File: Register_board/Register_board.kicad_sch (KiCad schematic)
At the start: 26 parts, among them J1 Conn_02x32_Odd_Even, U1 74LS374, U10 74LS181, U11 74LS181, U12 74LS374, U13 74LS374, U14 74LS374, U15 74LS374, U16 74LS244, U2 74LS374, U3 74LS374, U4 74LS374, U5 74LS244, U6 74LS374, U7 74LS374, U8 74LS244, U9 74LS75

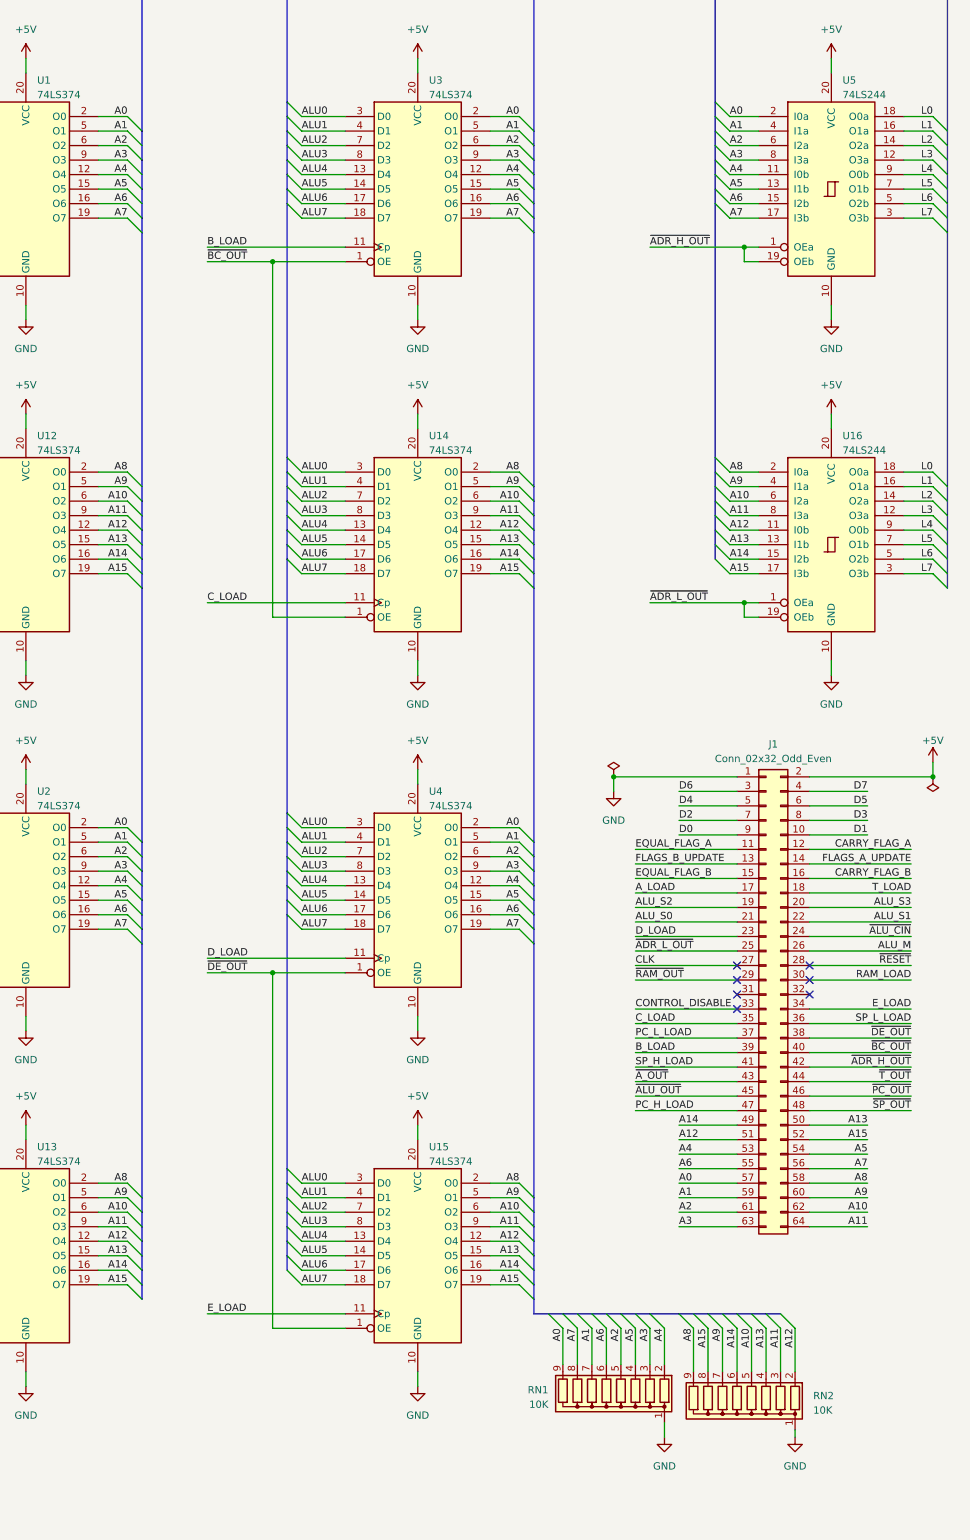
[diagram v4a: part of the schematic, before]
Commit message: Fix address line labelling error
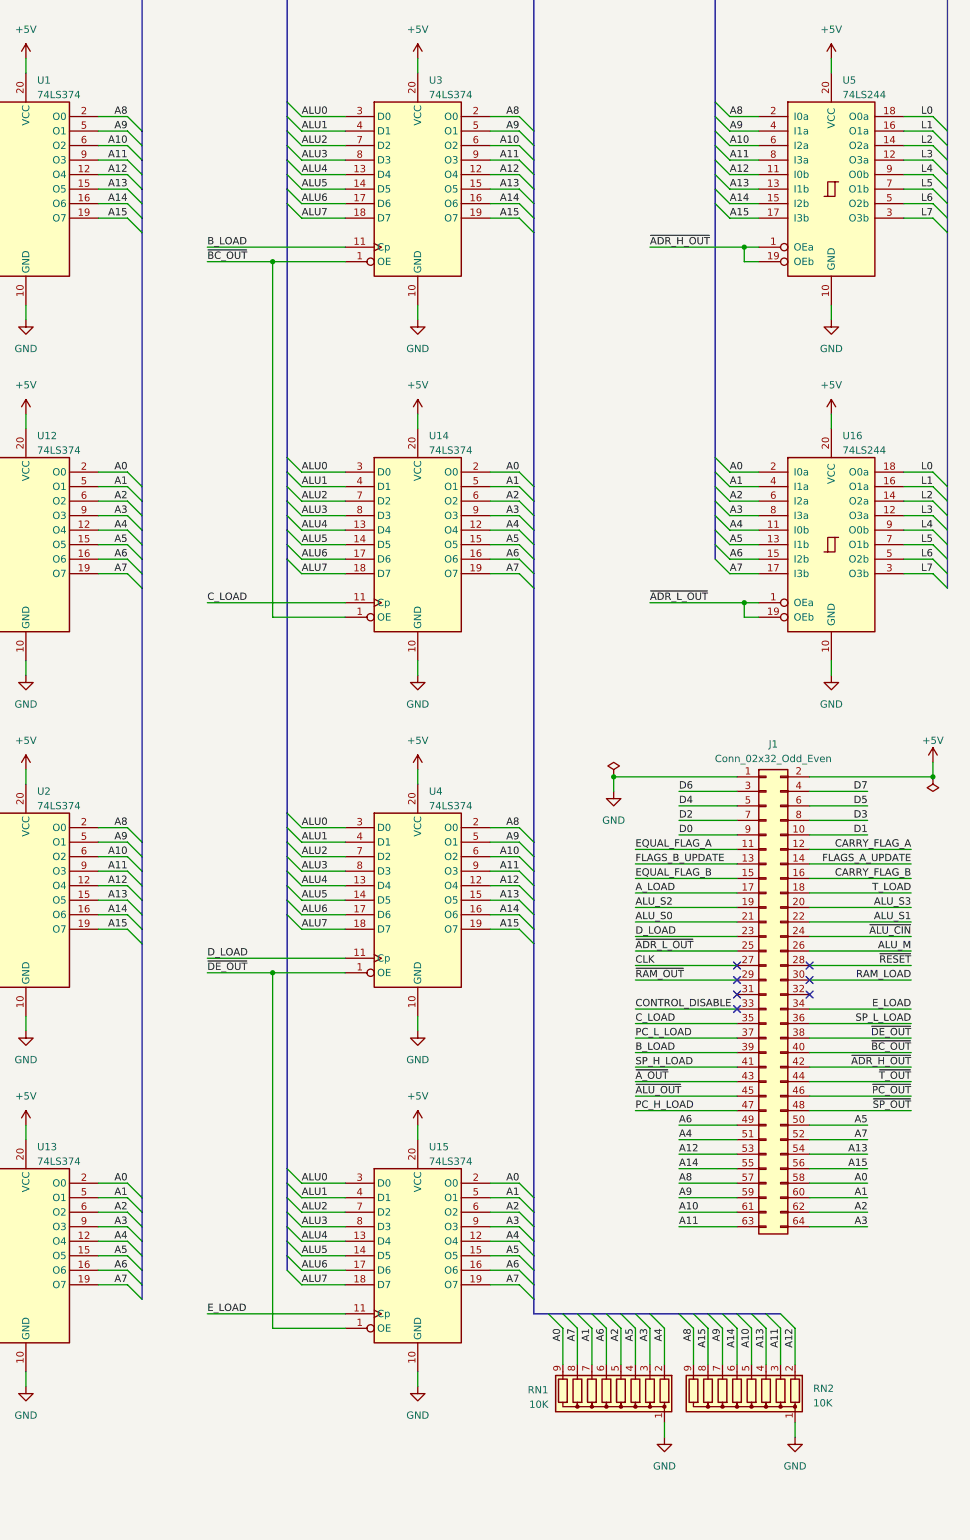
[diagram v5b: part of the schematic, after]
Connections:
- net A0: now also J1.58 (Pin_58), U12.2 (O0), U13.2 (O0), U14.2 (O0), U15.2 (O0), U16.2 (I0a); no longer J1.57 (Pin_57), U1.2 (O0), U2.2 (O0), U3.2 (O0), U4.2 (O0), U5.2 (I0a)
- net A1: now also J1.60 (Pin_60), U12.5 (O1), U13.5 (O1), U14.5 (O1), U15.5 (O1), U16.4 (I1a); no longer J1.59 (Pin_59), U1.5 (O1), U2.5 (O1), U3.5 (O1), U4.5 (O1), U5.4 (I1a)
- net A10: now also J1.61 (Pin_61), U1.6 (O2), U2.6 (O2), U3.6 (O2), U4.6 (O2), U5.6 (I2a); no longer J1.62 (Pin_62), U12.6 (O2), U13.6 (O2), U14.6 (O2), U15.6 (O2), U16.6 (I2a)
- net A11: now also J1.63 (Pin_63), U1.9 (O3), U2.9 (O3), U3.9 (O3), U4.9 (O3), U5.8 (I3a); no longer J1.64 (Pin_64), U12.9 (O3), U13.9 (O3), U14.9 (O3), U15.9 (O3), U16.8 (I3a)
- net A12: now also J1.53 (Pin_53), U1.12 (O4), U2.12 (O4), U3.12 (O4), U4.12 (O4), U5.11 (I0b); no longer J1.51 (Pin_51), U12.12 (O4), U13.12 (O4), U14.12 (O4), U15.12 (O4), U16.11 (I0b)
- net A13: now also J1.54 (Pin_54), U1.15 (O5), U2.15 (O5), U3.15 (O5), U4.15 (O5), U5.13 (I1b); no longer J1.50 (Pin_50), U12.15 (O5), U13.15 (O5), U14.15 (O5), U15.15 (O5), U16.13 (I1b)
- net A14: now also J1.55 (Pin_55), U1.16 (O6), U2.16 (O6), U3.16 (O6), U4.16 (O6), U5.15 (I2b); no longer J1.49 (Pin_49), U12.16 (O6), U13.16 (O6), U14.16 (O6), U15.16 (O6), U16.15 (I2b)
- net A15: now also J1.56 (Pin_56), U1.19 (O7), U2.19 (O7), U3.19 (O7), U4.19 (O7), U5.17 (I3b); no longer J1.52 (Pin_52), U12.19 (O7), U13.19 (O7), U14.19 (O7), U15.19 (O7), U16.17 (I3b)
- net A2: now also J1.62 (Pin_62), U12.6 (O2), U13.6 (O2), U14.6 (O2), U15.6 (O2), U16.6 (I2a); no longer J1.61 (Pin_61), U1.6 (O2), U2.6 (O2), U3.6 (O2), U4.6 (O2), U5.6 (I2a)
- net A3: now also J1.64 (Pin_64), U12.9 (O3), U13.9 (O3), U14.9 (O3), U15.9 (O3), U16.8 (I3a); no longer J1.63 (Pin_63), U1.9 (O3), U2.9 (O3), U3.9 (O3), U4.9 (O3), U5.8 (I3a)
- net A4: now also J1.51 (Pin_51), U12.12 (O4), U13.12 (O4), U14.12 (O4), U15.12 (O4), U16.11 (I0b); no longer J1.53 (Pin_53), U1.12 (O4), U2.12 (O4), U3.12 (O4), U4.12 (O4), U5.11 (I0b)
- net A5: now also J1.50 (Pin_50), U12.15 (O5), U13.15 (O5), U14.15 (O5), U15.15 (O5), U16.13 (I1b); no longer J1.54 (Pin_54), U1.15 (O5), U2.15 (O5), U3.15 (O5), U4.15 (O5), U5.13 (I1b)
- net A6: now also J1.49 (Pin_49), U12.16 (O6), U13.16 (O6), U14.16 (O6), U15.16 (O6), U16.15 (I2b); no longer J1.55 (Pin_55), U1.16 (O6), U2.16 (O6), U3.16 (O6), U4.16 (O6), U5.15 (I2b)
- net A7: now also J1.52 (Pin_52), U12.19 (O7), U13.19 (O7), U14.19 (O7), U15.19 (O7), U16.17 (I3b); no longer J1.56 (Pin_56), U1.19 (O7), U2.19 (O7), U3.19 (O7), U4.19 (O7), U5.17 (I3b)
- net A8: now also J1.57 (Pin_57), U1.2 (O0), U2.2 (O0), U3.2 (O0), U4.2 (O0), U5.2 (I0a); no longer J1.58 (Pin_58), U12.2 (O0), U13.2 (O0), U14.2 (O0), U15.2 (O0), U16.2 (I0a)
- net A9: now also J1.59 (Pin_59), U1.5 (O1), U2.5 (O1), U3.5 (O1), U4.5 (O1), U5.4 (I1a); no longer J1.60 (Pin_60), U12.5 (O1), U13.5 (O1), U14.5 (O1), U15.5 (O1), U16.4 (I1a)
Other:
- moved on the sheet: RN2

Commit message: Control board schematic done?
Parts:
- removed U9: 74LS75, Package_DIP:DIP-16_W7.62mm_Socket, symbol 74xx:74LS75
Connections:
- net CARRY_FLAG_A is gone; now on net CARRY_FLAG: J1.12 (Pin_12)
- net EQUAL_FLAG_A is gone; now on net EQUAL_FLAG: J1.11 (Pin_11)
- net EQUAL_FLAG: now reaches NT1.2, U11.14 (A=B)
- net CARRY_FLAG: now reaches U11.16 (Cn+4)
- net CARRY_FLAG_B: no longer names the net of J1.16 (Pin_16)
- net EQUAL_FLAG_B: no longer names the net of J1.15 (Pin_15)
- net FLAGS_A_UPDATE: no longer names the net of J1.14 (Pin_14)
- net FLAGS_B_UPDATE renamed INTERRUPT_FLAG
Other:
- note removed: "Latch bad, could cause control roms to oscilate Saves a chip over proper flip flops though"
